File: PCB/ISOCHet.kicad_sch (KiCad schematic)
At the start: 19 parts, among them J1 USB_C_Receptacle_USB2.0, J2 Conn_01x08_Pin, SW0 BOOT, SW1 TAB, SW2 ENTER, SW3 CAPS, SW4 CAPS_STEP1.5, SW5 CAPS_STEP1.25, U1 CH552G, U2 USBLC6-2P6

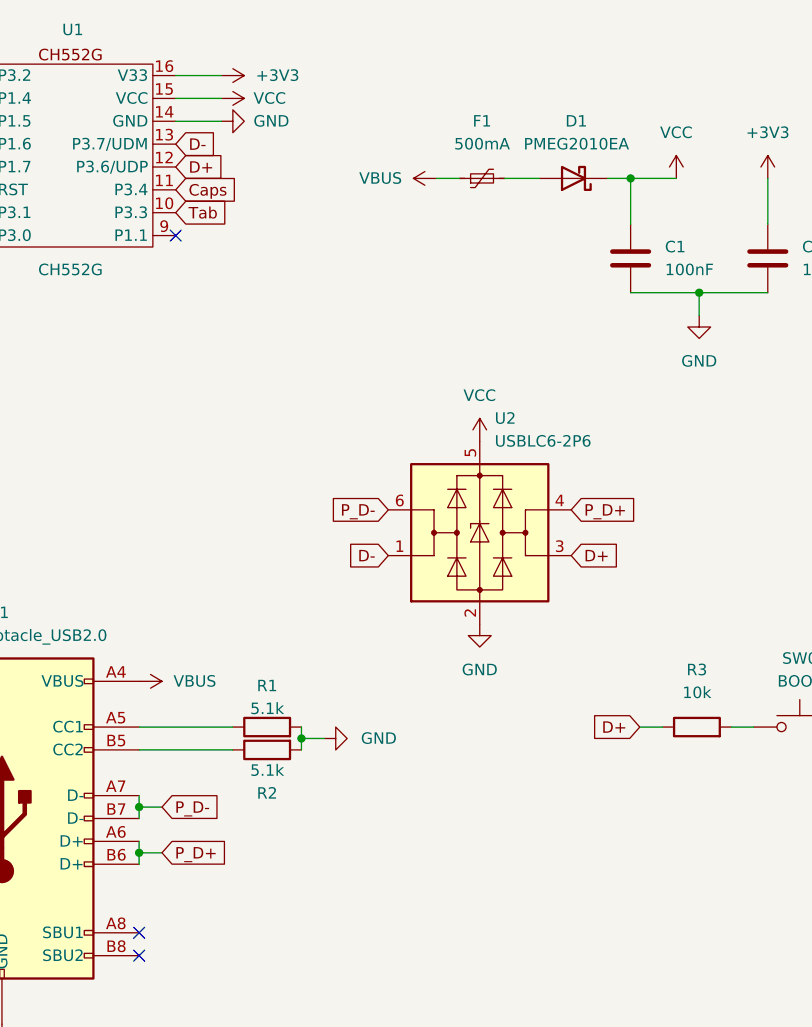
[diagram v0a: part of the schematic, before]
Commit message: Flip USB port to top side; add 3D models
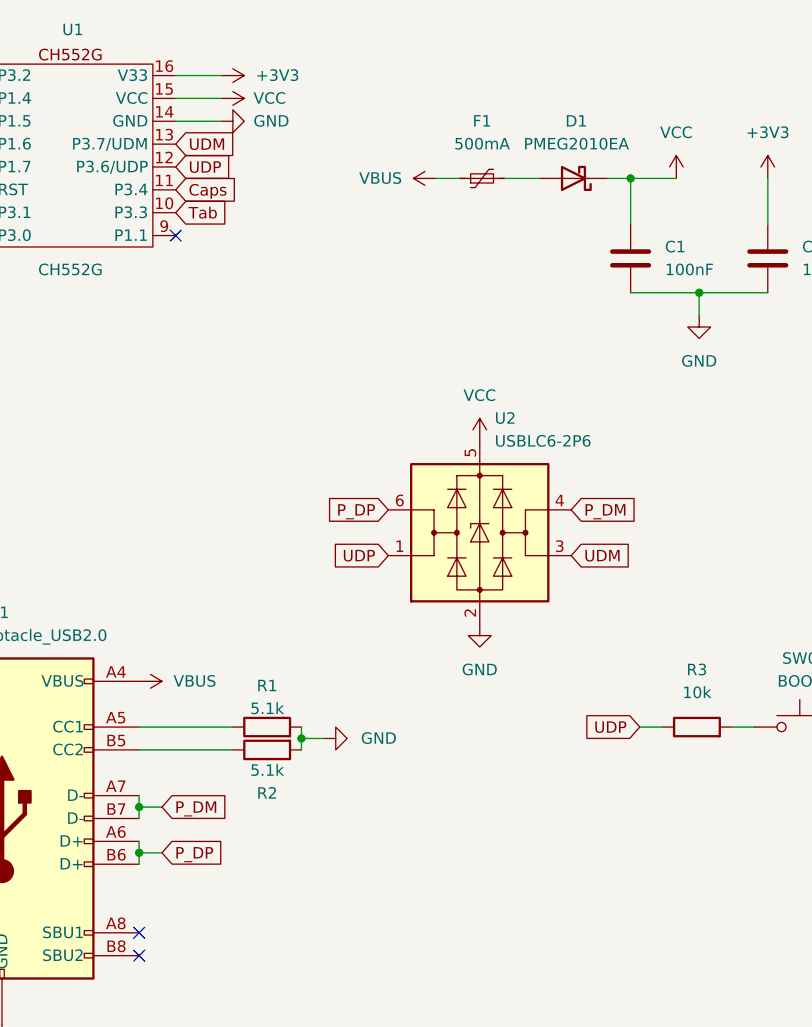
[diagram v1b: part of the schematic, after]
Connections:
- net D+ renamed UDP
- net UDP: now also U2.1 (I/O1); no longer U2.3 (I/O2)
- net D- renamed UDM
- net UDM: now also U2.3 (I/O2); no longer U2.1 (I/O1)
- net P_D+ renamed P_DP
- net P_DP: now also U2.6 (I/O1); no longer U2.4 (I/O2)
- net P_D- renamed P_DM
- net P_DM: now also U2.4 (I/O2); no longer U2.6 (I/O1)
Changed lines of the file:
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@@
     )
   )
-  (global_label "D+" (shape input) (at 65.024 46.99 0) (fields_autoplaced)
+  (global_label "UDP" (shape input) (at 65.024 46.99 0) (fields_autoplaced)
     (effects (font (size 1.27 1.27)) (justify left))
-    (property "Intersheetrefs" "${INTERSHEET_REFS}" (at 70.8516 46.99 0)
+    (property "Intersheetrefs" "${INTERSHEET_REFS}" (at 71.8797 46.99 0)
       (effects (font (size 1.27 1.27)) (justify left) hide)
     )
   )
-  (global_label "P_D-" (shape input) (at 88.646 85.09 180) (fields_autoplaced)
+  (global_label "P_DP" (shape input) (at 88.646 85.09 180) (fields_autoplaced)
     (effects (font (size 1.27 1.27)) (justify right))
-    (property "Intersheetrefs" "${INTERSHEET_REFS}" (at 80.5808 85.09 0)
+    (property "Intersheetrefs" "${INTERSHEET_REFS}" (at 80.8832 85.09 0)
       (effects (font (size 1.27 1.27)) (justify right) hide)
     )
@@
     )
   )
-  (global_label "P_D+" (shape input) (at 63.5 123.19 0) (fields_autoplaced)
+  (global_label "P_DP" (shape input) (at 63.5 123.19 0) (fields_autoplaced)
     (effects (font (size 1.27 1.27)) (justify left))
-    (property "Intersheetrefs" "${INTERSHEET_REFS}" (at 71.5652 123.19 0)
+    (property "Intersheetrefs" "${INTERSHEET_REFS}" (at 71.2628 123.19 0)
       (effects (font (size 1.27 1.27)) (justify left) hide)
     )
   )
-  (global_label "P_D+" (shape input) (at 108.966 85.09 0) (fields_autoplaced)
+  (global_label "P_DM" (shape input) (at 108.966 85.09 0) (fields_autoplaced)
     (effects (font (size 1.27 1.27)) (justify left))
-    (property "Intersheetrefs" "${INTERSHEET_REFS}" (at 117.0312 85.09 0)
+    (property "Intersheetrefs" "${INTERSHEET_REFS}" (at 116.9102 85.09 0)
       (effects (font (size 1.27 1.27)) (justify left) hide)
     )
   )
-  (global_label "D-" (shape input) (at 88.646 90.17 180) (fields_autoplaced)
+  (global_label "UDP" (shape input) (at 88.646 90.17 180) (fields_autoplaced)
     (effects (font (size 1.27 1.27)) (justify right))
-    (property "Intersheetrefs" "${INTERSHEET_REFS}" (at 82.8184 90.17 0)
+    (property "Intersheetrefs" "${INTERSHEET_REFS}" (at 81.7903 90.17 0)
       (effects (font (size 1.27 1.27)) (justify right) hide)
     )
@@
     )
   )
-  (global_label "P_D-" (shape input) (at 63.5 118.11 0) (fields_autoplaced)
+  (global_label "P_DM" (shape input) (at 63.5 118.11 0) (fields_autoplaced)
     (effects (font (size 1.27 1.27)) (justify left))
-    (property "Intersheetrefs" "${INTERSHEET_REFS}" (at 71.5652 118.11 0)
+    (property "Intersheetrefs" "${INTERSHEET_REFS}" (at 71.4442 118.11 0)
       (effects (font (size 1.27 1.27)) (justify left) hide)
     )
@@
     )
   )
-  (global_label "D+" (shape input) (at 116.586 109.22 180) (fields_autoplaced)
+  (global_label "UDP" (shape input) (at 116.586 109.22 180) (fields_autoplaced)
     (effects (font (size 1.27 1.27)) (justify right))
-    (property "Intersheetrefs" "${INTERSHEET_REFS}" (at 110.7584 109.22 0)
+    (property "Intersheetrefs" "${INTERSHEET_REFS}" (at 109.7303 109.22 0)
       (effects (font (size 1.27 1.27)) (justify right) hide)
     )
@@
     )
   )
-  (global_label "D+" (shape input) (at 108.966 90.17 0) (fields_autoplaced)
+  (global_label "UDM" (shape input) (at 108.966 90.17 0) (fields_autoplaced)
     (effects (font (size 1.27 1.27)) (justify left))
-    (property "Intersheetrefs" "${INTERSHEET_REFS}" (at 114.7936 90.17 0)
+    (property "Intersheetrefs" "${INTERSHEET_REFS}" (at 116.0031 90.17 0)
       (effects (font (size 1.27 1.27)) (justify left) hide)
     )
   )
-  (global_label "D-" (shape input) (at 65.024 44.45 0) (fields_autoplaced)
+  (global_label "UDM" (shape input) (at 65.024 44.45 0) (fields_autoplaced)
     (effects (font (size 1.27 1.27)) (justify left))
-    (property "Intersheetrefs" "${INTERSHEET_REFS}" (at 70.8516 44.45 0)
+    (property "Intersheetrefs" "${INTERSHEET_REFS}" (at 72.0611 44.45 0)
       (effects (font (size 1.27 1.27)) (justify left) hide)
     )

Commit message: Add LSCC part numbers; add 3D models for MX switches and stabiliser
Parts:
- C1, C2: LSCC (none) -> C1525
- D1: LSCC (none) -> C2837790
- F1: LSCC (none) -> C210357
- H1, H2, J2, SW1, SW2, SW3, SW4, SW5: now left out of the parts list
- R1, R2: LSCC (none) -> C25905
- R3: LSCC (none) -> C25744
- SW0: LSCC (none) -> C221821
- U1: LSCC (none) -> C111292
- U2: LSCC (none) -> C2687116
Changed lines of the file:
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@@
   )
   (symbol (lib_id "Switch:SW_Push") (at 198.12 83.82 0) (unit 1)
-    (in_bom yes) (on_board yes) (dnp no) (fields_autoplaced)
+    (in_bom no) (on_board yes) (dnp no) (fields_autoplaced)
     (property "Reference" "SW2" (at 198.12 76.2 0)
       (effects (font (size 1.27 1.27)))
@@
     )
     (property "Datasheet" "~" (at 122.936 109.22 0)
+      (effects (font (size 1.27 1.27)) hide)
+    )
+    (property "LSCC" "C25744" (at 122.936 109.22 90)
       (effects (font (size 1.27 1.27)) hide)
     )
@@
       (effects (font (size 1.27 1.27)) hide)
     )
+    (property "LSCC" "C2687116" (at 98.806 87.63 0)
+      (effects (font (size 1.27 1.27)) hide)
+    )
     (pin "2")
     (pin "1")
@@
   )
   (symbol (lib_id "Mechanical:MountingHole_Pad") (at 40.64 177.8 0) (unit 1)
-    (in_bom yes) (on_board yes) (dnp no) (fields_autoplaced)
+    (in_bom no) (on_board yes) (dnp no) (fields_autoplaced)
     (property "Reference" "H1" (at 43.18 175.26 0)
       (effects (font (size 1.27 1.27)) (justify left))
@@
   )
   (symbol (lib_id "Switch:SW_Push") (at 264.16 81.28 0) (unit 1)
-    (in_bom yes) (on_board yes) (dnp no) (fields_autoplaced)
+    (in_bom no) (on_board yes) (dnp no) (fields_autoplaced)
     (property "Reference" "SW5" (at 264.16 73.66 0)
       (effects (font (size 1.27 1.27)))
@@
   )
   (symbol (lib_id "Switch:SW_Push") (at 243.84 81.28 0) (unit 1)
-    (in_bom yes) (on_board yes) (dnp no) (fields_autoplaced)
+    (in_bom no) (on_board yes) (dnp no) (fields_autoplaced)
     (property "Reference" "SW4" (at 243.84 73.66 0)
       (effects (font (size 1.27 1.27)))
@@
   )
   (symbol (lib_id "Switch:SW_Push") (at 220.98 81.28 0) (unit 1)
-    (in_bom yes) (on_board yes) (dnp no) (fields_autoplaced)
+    (in_bom no) (on_board yes) (dnp no) (fields_autoplaced)
     (property "Reference" "SW3" (at 220.98 73.66 0)
       (effects (font (size 1.27 1.27)))
@@
       (effects (font (size 1.27 1.27)) hide)
     )
+    (property "LSCC" "C25905" (at 75.184 109.22 90)
+      (effects (font (size 1.27 1.27)) hide)
+    )
     (pin "1")
     (pin "2")
@@
     )
     (property "Datasheet" "~" (at 109.22 48.26 0)
+      (effects (font (size 1.27 1.27)) hide)
+    )
+    (property "LSCC" "C2837790" (at 109.22 48.26 0)
       (effects (font (size 1.27 1.27)) hide)
     )
@@
     )
     (property "Datasheet" "~" (at 99.06 48.26 0)
+      (effects (font (size 1.27 1.27)) hide)
+    )
+    (property "LSCC" "C210357" (at 99.06 48.26 90)
       (effects (font (size 1.27 1.27)) hide)
     )
@@
       (effects (font (size 1.27 1.27)) hide)
     )
+    (property "LSCC" "C221821" (at 134.366 109.22 0)
+      (effects (font (size 1.27 1.27)) hide)
+    )
     (pin "1")
     (pin "2")
@@
   )
   (symbol (lib_id "Switch:SW_Push") (at 170.18 83.82 0) (unit 1)
-    (in_bom yes) (on_board yes) (dnp no) (fields_autoplaced)
+    (in_bom no) (on_board yes) (dnp no) (fields_autoplaced)
     (property "Reference" "SW1" (at 170.18 76.2 0)
       (effects (font (size 1.27 1.27)))
@@
   )
   (symbol (lib_id "Mechanical:MountingHole") (at 40.64 190.5 0) (unit 1)
-    (in_bom yes) (on_board yes) (dnp no)
+    (in_bom no) (on_board yes) (dnp no)
     (property "Reference" "H2" (at 43.18 189.23 0)
       (effects (font (size 1.27 1.27)) (justify left))
@@
       (effects (font (size 1.27 1.27)) hide)
     )
+    (property "LSCC" "C1525" (at 115.57 57.15 0)
+      (effects (font (size 1.27 1.27)) hide)
+    )
     (pin "1")
     (pin "2")
@@
   )
   (symbol (lib_id "Connector:Conn_01x08_Pin") (at 21.844 49.53 0) (mirror x) (unit 1)
-    (in_bom yes) (on_board yes) (dnp no)
+    (in_bom no) (on_board yes) (dnp no)
     (property "Reference" "J2" (at 22.479 62.23 0)
       (effects (font (size 1.27 1.27)))
@@
       (effects (font (size 1.27 1.27)) hide)
     )
+    (property "LSCC" "C1525" (at 130.81 57.15 0)
+      (effects (font (size 1.27 1.27)) hide)
+    )
     (pin "1")
     (pin "2")
@@
       (effects (font (size 1.27 1.27)) hide)
     )
+    (property "LSCC" "C25905" (at 75.184 111.76 90)
+      (effects (font (size 1.27 1.27)) hide)
+    )
     (pin "1")
     (pin "2")
@@
       (effects (font (size 1.27 1.27)) hide)
     )
+    (property "LSCC" "C111292" (at 53.34 45.72 0)
+      (effects (font (size 1.27 1.27)) hide)
+    )

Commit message: Rotate ISO stabiliser, improve STEP export
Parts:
- H2: footprint PCM_marbastlib-mx:STAB_MX_P_ISO -> PCM_marbastlib-mx:STAB_MX_P_ISO-ROT; now in the parts list
- SW1, SW2, SW3: now in the parts list
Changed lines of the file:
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@@
   )
   (symbol (lib_id "Switch:SW_Push") (at 198.12 83.82 0) (unit 1)
-    (in_bom no) (on_board yes) (dnp no) (fields_autoplaced)
+    (in_bom yes) (on_board yes) (dnp no) (fields_autoplaced)
     (property "Reference" "SW2" (at 198.12 76.2 0)
       (effects (font (size 1.27 1.27)))
@@
   )
   (symbol (lib_id "Switch:SW_Push") (at 220.98 81.28 0) (unit 1)
-    (in_bom no) (on_board yes) (dnp no) (fields_autoplaced)
+    (in_bom yes) (on_board yes) (dnp no) (fields_autoplaced)
     (property "Reference" "SW3" (at 220.98 73.66 0)
       (effects (font (size 1.27 1.27)))
@@
   )
   (symbol (lib_id "Switch:SW_Push") (at 170.18 83.82 0) (unit 1)
-    (in_bom no) (on_board yes) (dnp no) (fields_autoplaced)
+    (in_bom yes) (on_board yes) (dnp no) (fields_autoplaced)
     (property "Reference" "SW1" (at 170.18 76.2 0)
       (effects (font (size 1.27 1.27)))
@@
   )
   (symbol (lib_id "Mechanical:MountingHole") (at 40.64 190.5 0) (unit 1)
-    (in_bom no) (on_board yes) (dnp no)
+    (in_bom yes) (on_board yes) (dnp no)
     (property "Reference" "H2" (at 43.18 189.23 0)
       (effects (font (size 1.27 1.27)) (justify left))
@@
       (effects (font (size 1.27 1.27)) (justify left))
     )
-    (property "Footprint" "PCM_marbastlib-mx:STAB_MX_P_ISO" (at 40.64 190.5 0)
-      (effects (font (size 1.27 1.27)) hide)
-    )
+    (property "Footprint" "PCM_marbastlib-mx:STAB_MX_P_ISO-ROT" (at 40.64 190.5 0)
+      (effects (font (size 1.27 1.27)) hide)
+    )
